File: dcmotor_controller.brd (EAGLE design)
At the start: 142.2 x 90.6 mm, 81 parts, among them IC1 L298, IC2 L298, IC5 SN74LVCR162245A, Q1 MOSFET-PCHANNEL_SOT23-3, Q2 8MHz, T1 BC857BS, T14 BSS306N, U2 STM32F10XRXT6

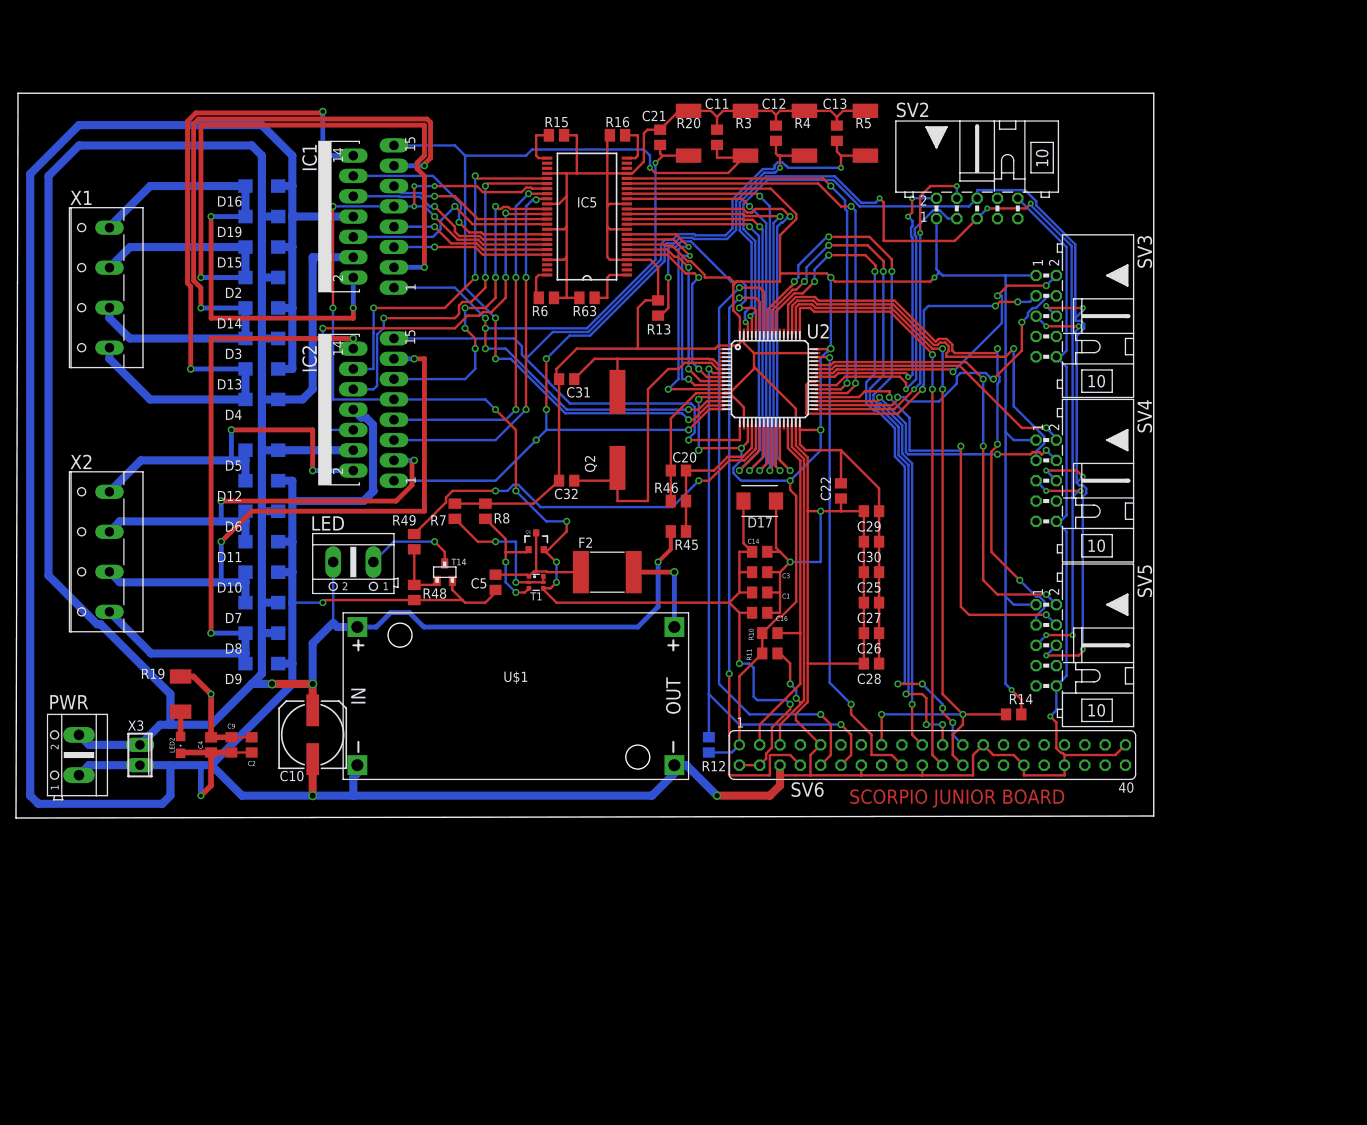
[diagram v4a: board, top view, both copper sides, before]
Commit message: poprawione umiejscowienie kondensatorów
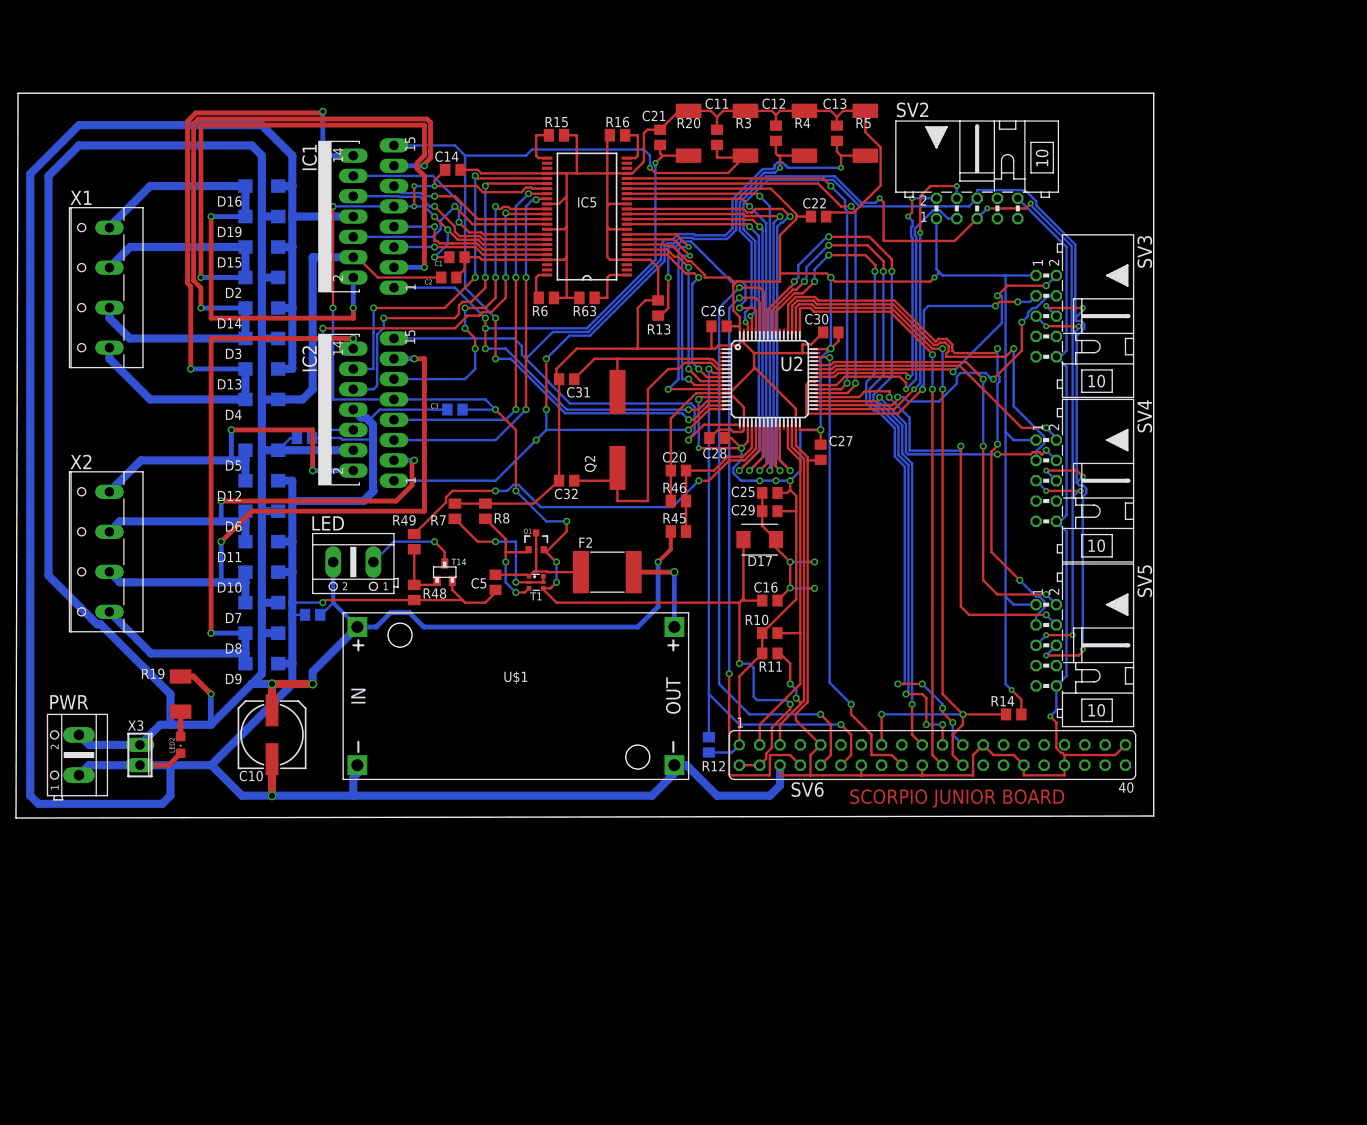
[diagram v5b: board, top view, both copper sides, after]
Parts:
- moved C2 63.4 mm to (53.8, 67.3), turned to 0 degrees
- moved C14 61.2 mm to (54.4, 80.8)
- moved C1 56.5 mm to (54.9, 69.8)
- moved C3 43.2 mm to (54.6, 50.8), flipped to the bottom
- moved C26 42.8 mm to (87.6, 61.2)
- moved C4 40.1 mm to (35.8, 47.2), flipped to the bottom, turned to 180 degrees
- moved C22 34.4 mm to (100.1, 74.9), turned to 180 degrees
- moved C28 34.2 mm to (87.4, 47.2)
- moved C30 26.7 mm to (101.6, 60.5)
- moved C27 19.8 mm to (100.3, 45.5), turned to 270 degrees
- moved C9 19.2 mm to (36.8, 25.1), flipped to the bottom, turned to 0 degrees
- moved C25 16.1 mm to (94.0, 40.4)
- moved C29 12.7 mm to (94.0, 38.1)
- moved C10 5.08 mm to (31.8, 10.2)
- moved D17 4.83 mm to (92.7, 34.5)
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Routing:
- net 3V3: track 307.1 -> 282.5 mm, vias 9 -> 11
- net GND: track 875.1 -> 896.4 mm
- net 24V: track 347.7 -> 353.7 mm
- net 5V: track 198.8 -> 202.8 mm, vias 13 -> 15
- net SEN4: track 114.6 -> 113.5 mm
- net IN12: track 20.3 -> 21.4 mm
- net B_DIR_V3: vias 2 -> 1

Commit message: mini poprawka
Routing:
- net 3V3: vias 11 -> 9
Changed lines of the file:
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@@
 <wire x1="91.23" y1="48.91" x2="91.23" y2="46.78" width="0.3048" layer="1"/>
 <wire x1="91.23" y1="46.78" x2="90.424" y2="45.974" width="0.3048" layer="1"/>
-<wire x1="90.368025" y1="41.91" x2="92.71" y2="41.91" width="0.3048" layer="16"/>
-<wire x1="92.71" y1="41.91" x2="94.742" y2="41.91" width="0.3048" layer="16"/>
+<wire x1="90.368025" y1="41.91" x2="96.52" y2="41.91" width="0.3048" layer="16"/>
 <via x="96.52" y="41.91" extent="1-16" drill="0.5"/>
-<wire x1="94.742" y1="41.91" x2="96.52" y2="41.91" width="0.3048" layer="16"/>
 <wire x1="97.278" y1="38.1" x2="97.278" y2="40.0016" width="0.3048" layer="1"/>
 <wire x1="97.278" y1="40.0016" x2="96.52" y2="40.7596" width="0.3048" layer="1"/>
@@
 <wire x1="89.154" y1="47.244" x2="88.326" y2="47.244" width="0.3048" layer="1"/>
 <wire x1="99.126" y1="74.93" x2="97.278" y2="74.93" width="0.3048" layer="1"/>
-<via x="94.742" y="41.91" extent="1-16" drill="0.5"/>
-<via x="92.71" y="41.91" extent="1-16" drill="0.5"/>
 <wire x1="94.93" y1="40.386" x2="96.1464" y2="40.386" width="0.3048" layer="1"/>
 <wire x1="96.1464" y1="40.386" x2="96.52" y2="40.7596" width="0.3048" layer="1"/>

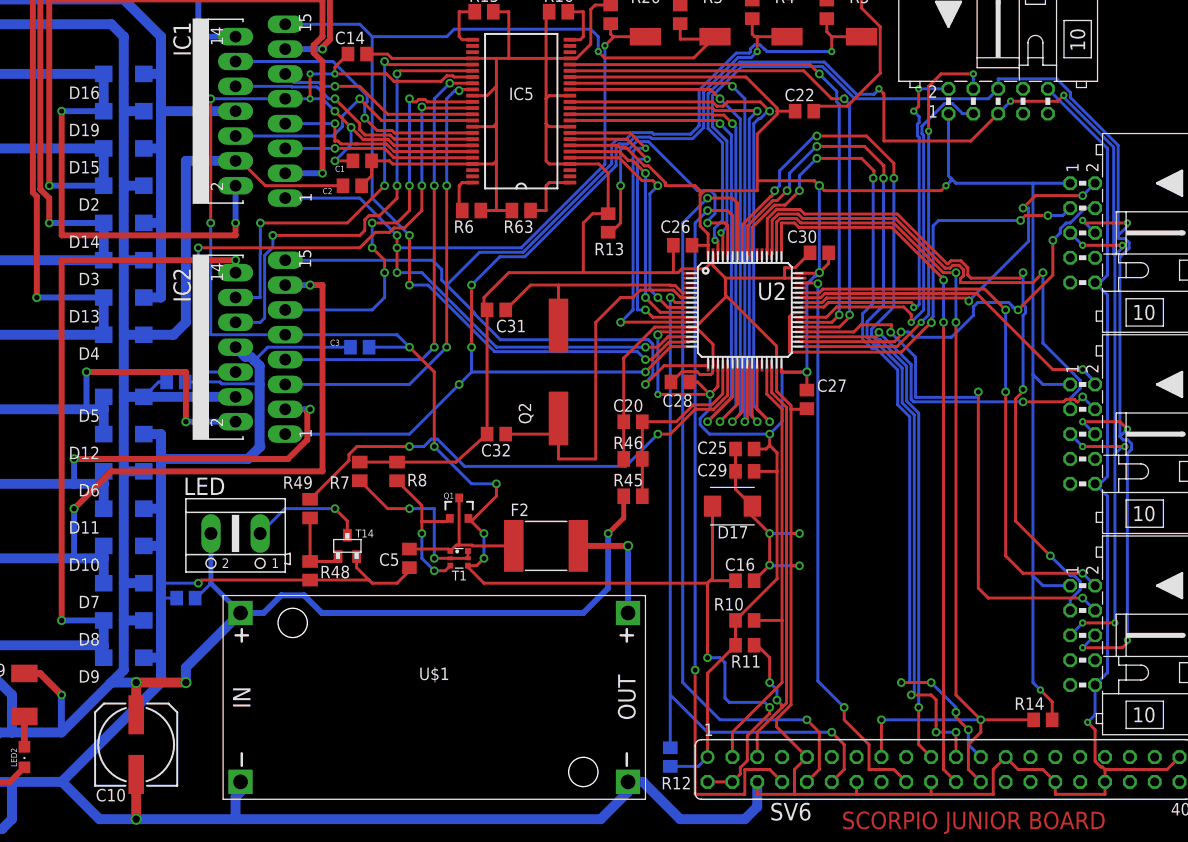
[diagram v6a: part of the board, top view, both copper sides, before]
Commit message: poprawione przelotki
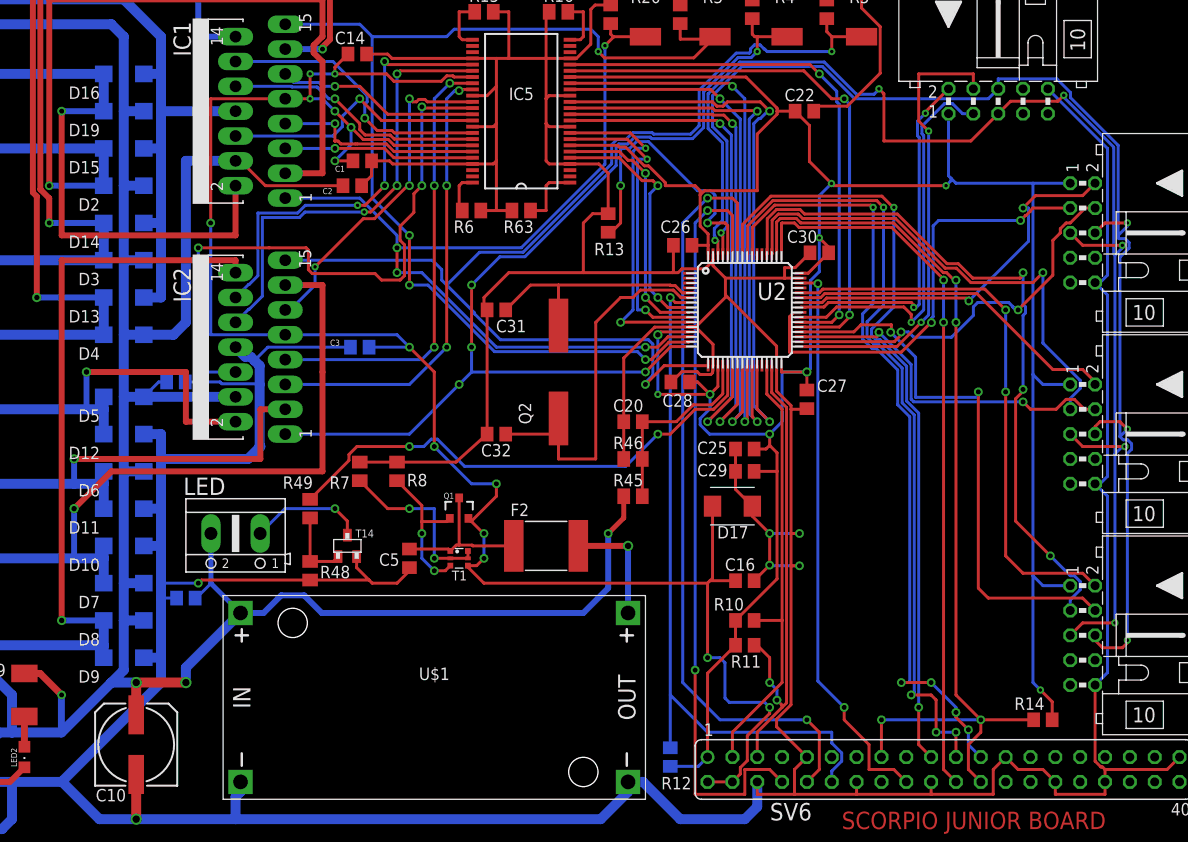
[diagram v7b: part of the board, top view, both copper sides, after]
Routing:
- net RPI_MOSI: track 89.2 -> 80.2 mm, vias 4 -> 2
- net RPI_MISO: track 89.8 -> 81.7 mm, vias 6 -> 4
- net RPI_CLK: track 88.2 -> 81.0 mm, vias 7 -> 5
- net PWM_SIGNAL3: track 56.8 -> 63.9 mm
- net CLK: track 141.3 -> 134.2 mm, vias 7 -> 4
- net PWM_SIGNAL4: track 41.4 -> 34.7 mm, vias 5 -> 3
- net MOT32: track 54.3 -> 50.6 mm, vias 2 -> 1
- net 3V3: track 282.5 -> 285.2 mm
- net A_LSB_U1: track 38.5 -> 36.3 mm, vias 3 -> 2
- net INDEX_W1: track 44.4 -> 46.6 mm, vias 3 -> 2
- net B_DIR_V3: track 52.2 -> 50.7 mm
- net IN41: track 47.4 -> 46.3 mm
- net IN42: track 46.2 -> 45.6 mm
- net B_DIR_V4: track 72.6 -> 71.9 mm
- net GND: track 896.4 -> 895.7 mm, vias 7 -> 6
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
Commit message: plus mała poprawka
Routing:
- net SEN3: vias 5 -> 4
- net N$24: vias 1 -> 0
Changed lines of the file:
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@@
 <wire x1="86.42" y1="50.86" x2="83.82" y2="48.26" width="0.3048" layer="1"/>
 <via x="83.82" y="48.26" extent="1-16" drill="0.5"/>
-<wire x1="66.04" y1="48.26" x2="64.77" y2="46.99" width="0.3048" layer="16"/>
 <wire x1="83.82" y1="48.26" x2="66.04" y2="48.26" width="0.3048" layer="16"/>
-<via x="64.77" y="46.99" extent="1-16" drill="0.5"/>
 <wire x1="46.99" y1="41.91" x2="59.69" y2="41.91" width="0.3048" layer="16"/>
-<wire x1="59.69" y1="41.91" x2="64.77" y2="46.99" width="0.3048" layer="16"/>
+<wire x1="59.69" y1="41.91" x2="66.04" y2="48.26" width="0.3048" layer="16"/>
 <contactref element="C12" pad="2"/>
 <contactref element="R4" pad="2"/>
@@
 <wire x1="53.34" y1="31.58" x2="53.34" y2="33.02" width="0.3048" layer="1"/>
 <wire x1="53.34" y1="33.02" x2="52.07" y2="34.29" width="0.3048" layer="1"/>
-<via x="52.07" y="34.29" extent="1-16" drill="0.5"/>
-<wire x1="52.07" y1="34.29" x2="46.9646" y2="34.29" width="0.3048" layer="16"/>
-<wire x1="46.9646" y1="34.29" x2="44.4246" y2="31.75" width="0.3048" layer="16"/>
+<wire x1="52.07" y1="34.29" x2="46.9646" y2="34.29" width="0.3048" layer="1"/>
+<wire x1="46.9646" y1="34.29" x2="44.4246" y2="31.75" width="0.3048" layer="1"/>
 </signal>
 <signal name="+3V3">
